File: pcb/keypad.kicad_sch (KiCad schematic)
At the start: 54 parts, among them J1 Conn_02x06_Odd_Even, SW1 SW_Push, SW10 SW_Push, SW11 SW_Push, SW12 SW_Push, SW13 SW_Push, SW14 SW_Push, SW15 SW_Push, SW16 SW_Push, SW17 SW_Push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

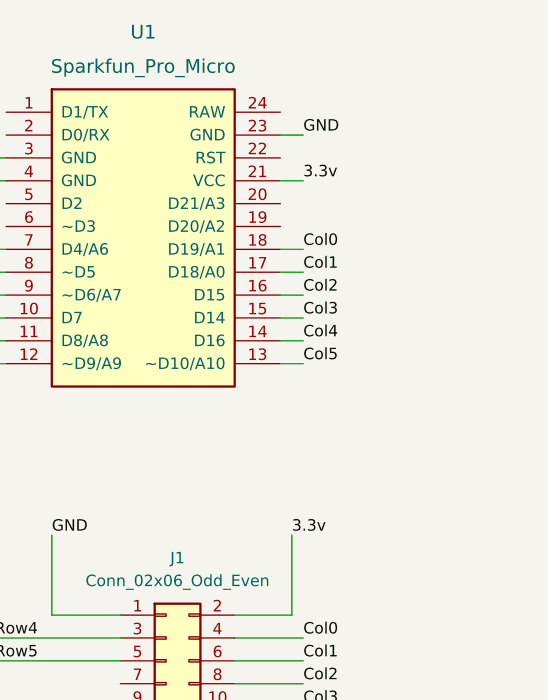
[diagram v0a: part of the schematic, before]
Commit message: - Added a reset button for the controller  - Moved the through-hole diodes to not interfere with the switches
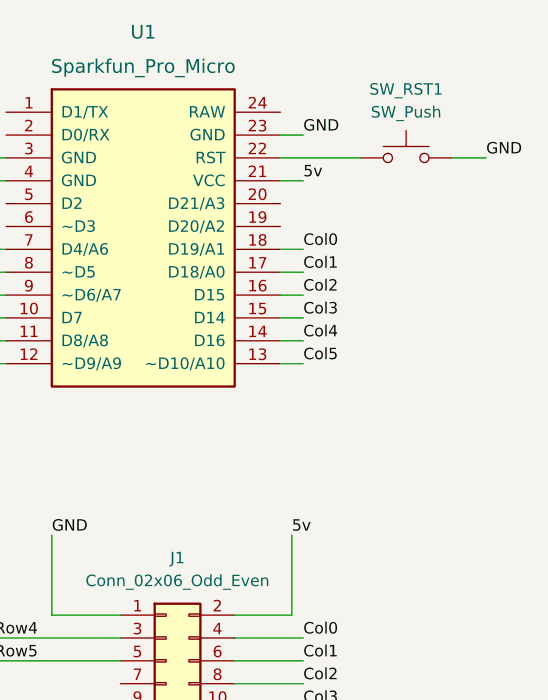
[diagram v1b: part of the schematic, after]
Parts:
- added SW_RST1: SW_Push, Button_Switch_THT:SW_PUSH_6mm_H7.3mm, symbol Switch:SW_Push
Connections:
- net GND: now also SW_RST1.2
- net at U1.22 (RST): now also SW_RST1.1
- net 3.3v renamed 5v
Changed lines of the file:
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@@
+    (stroke (width 0) (type default) (color 0 0 0 0))
+  )
+  (wire (pts (xy 204.47 36.83) (xy 208.28 36.83))
     (stroke (width 0) (type default) (color 0 0 0 0))
   )
@@
     (stroke (width 0) (type default) (color 0 0 0 0))
   )
+  (wire (pts (xy 185.42 36.83) (xy 194.31 36.83))
+    (stroke (width 0) (type default) (color 0 0 0 0))
+  )
   (wire (pts (xy 153.67 92.71) (xy 167.64 92.71))
     (stroke (width 0) (type default) (color 0 0 0 0))
@@
     (effects (font (size 1.27 1.27)) (justify left bottom))
   )
-  (label "3.3v" (at 187.96 39.37 0)
+  (label "5v" (at 187.96 39.37 0)
     (effects (font (size 1.27 1.27)) (justify left bottom))
   )
@@
     (effects (font (size 1.27 1.27)) (justify left bottom))
   )
+  (label "GND" (at 208.28 36.83 0)
+    (effects (font (size 1.27 1.27)) (justify left bottom))
+  )
   (label "Col2" (at 187.96 95.25 0)
     (effects (font (size 1.27 1.27)) (justify left bottom))
@@
     (effects (font (size 1.27 1.27)) (justify left bottom))
   )
-  (label "3.3v" (at 186.69 78.74 0)
+  (label "5v" (at 186.69 78.74 0)
     (effects (font (size 1.27 1.27)) (justify left bottom))
   )
@@
     )
     (property "Datasheet" "~" (id 3) (at 44.45 66.04 0)
+      (effects (font (size 1.27 1.27)) hide)
+    )
+    (pin "1")
+    (pin "2")
+  )
+  (symbol (lib_id "Switch:SW_Push") (at 199.39 36.83 0) (unit 1)
+    (in_bom yes) (on_board yes)
+    (property "Reference" "SW_RST1" (id 0) (at 199.39 29.21 0))
+    (property "Value" "SW_Push" (id 1) (at 199.39 31.75 0))
+    (property "Footprint" "Button_Switch_THT:SW_PUSH_6mm_H7.3mm" (id 2) (at 199.39 31.75 0)
+      (effects (font (size 1.27 1.27)) hide)
+    )
+    (property "Datasheet" "~" (id 3) (at 199.39 31.75 0)
       (effects (font (size 1.27 1.27)) hide)
     )
@@
       (reference "SW_C1") (unit 1) (value "SW_Push") (footprint "Button_Switch_THT:SW_PUSH_6mm_H7.3mm")
     )
+    (path "/5b2e8b2b-3715-432b-9074-5bf4a85d40d6"
+      (reference "SW_RST1") (unit 1) (value "SW_Push") (footprint "Button_Switch_THT:SW_PUSH_6mm_H7.3mm")
+    )
     (path "/7127a1b5-5c6f-4116-ab41-a3e00f7558f8"

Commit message: - Switched to the KB2040  - Modified the pin header to remove some silk screen sections
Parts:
- removed U1: Sparkfun_Pro_Micro, Arduino:Sparkfun_Pro_Micro, symbol Arduino:Sparkfun_Pro_Micro
- added U1: kb2040, kb2040:kb2040, symbol kb2040:kb2040
- J1: footprint Connector_PinHeader_2.54mm:PinHeader_2x06_P2.54mm_Horizontal -> keypad:PinHeader_2x06_P2.54mm_Horizontal
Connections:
- net Col0: now also U1.21 (A1/27)
- net Col1: now also U1.22 (A0/26)
- net Col2: now also U1.23 (SCK/18)
- net Col3: now also U1.24 (MISO/20)
- net Col4: now also U1.25 (MOSI/19)
- net Col5: now also U1.26 (D10)
- net GND: now also U1.16 (GND), U1.4 (GND), U1.5 (GND)
- net Row0: now also U1.13 (D9)
- net Row1: now also U1.12 (D8)
- net Row2: now also U1.11 (D7)
- net Row3: now also U1.10 (D6)
- net Row4: now also U1.9 (D5)
- net Row5: now also U1.8 (D4)
- net at SW_RST1.1: now also U1.17 (RESET)
- net 5v renamed 3.3v
- net 3.3v: now also U1.18 (3.3v)

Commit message: Moved necessary symbols into the project library  - (I don't know if this comes with license issues; if there's a problem let me know and I can remove the symbols)
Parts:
- SW1, SW10, SW11, SW12, SW13, SW14, SW16, SW17, SW18, SW2, SW21, SW3, SW4, SW5, SW6, SW7, SW8, SW9: footprint MX_Only:MXOnly-1U-Hotswap -> keypad:MXOnly-1U-Hotswap
- SW15, SW19: footprint MX_Only:MXOnly-1.25U-Hotswap -> keypad:MXOnly-1.25U-Hotswap
- SW20, SW22: footprint MX_Only:MXOnly-2U-Hotswap -> keypad:MXOnly-2U-Hotswap
- U1: footprint kb2040:kb2040 -> keypad:kb2040; symbol kb2040:kb2040 -> keypad:kb2040

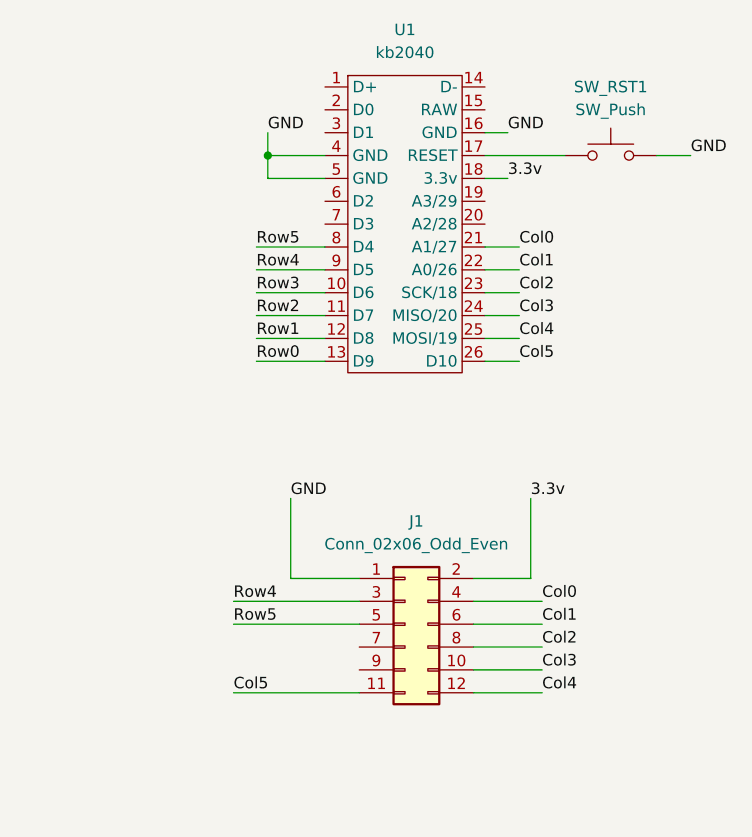
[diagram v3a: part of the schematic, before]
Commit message: - Marked NC pins  - Updated diode symbols
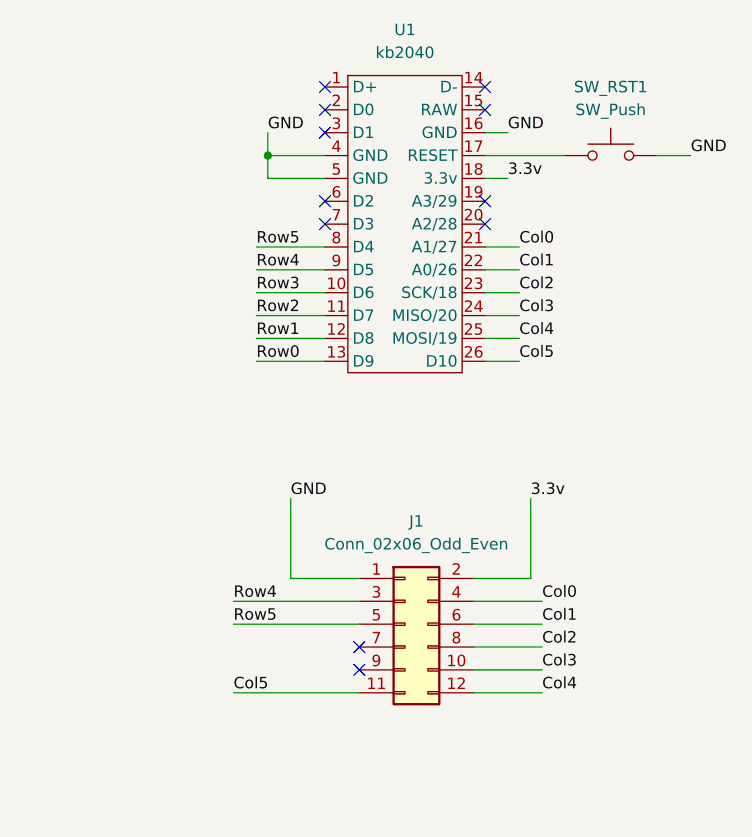
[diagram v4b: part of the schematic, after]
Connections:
- no-connect marks 0 -> 11
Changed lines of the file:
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@@
   (junction (at 100.33 59.69) (diameter 0) (color 0 0 0 0)
   )
+  (no_connect (at 167.64 97.79))
+  (no_connect (at 163.83 33.02))
+  (no_connect (at 163.83 38.1))
+  (no_connect (at 163.83 35.56))
+  (no_connect (at 163.83 48.26))
+  (no_connect (at 181.61 45.72))
+  (no_connect (at 163.83 45.72))
+  (no_connect (at 181.61 33.02))
+  (no_connect (at 181.61 48.26))
+  (no_connect (at 167.64 95.25))
+  (no_connect (at 181.61 35.56))
   (wire (pts (xy 71.12 53.34) (xy 67.31 53.34))
     (stroke (width 0) (type default) (color 0 0 0 0))
@@
     (effects (font (size 1.27 1.27)) (justify left bottom))
   )
-  (symbol (lib_id "Diode:1N4148") (at 120.65 105.41 0) (unit 1)
+  (symbol (lib_name "1N4148_10") (lib_id "Diode:1N4148") (at 120.65 105.41 0) (unit 1)
     (in_bom yes) (on_board yes) (fields_autoplaced)
     (property "Reference" "D18" (id 0) (at 120.65 99.06 0))
@@
     (pin "2")
   )
-  (symbol (lib_id "Diode:1N4148") (at 74.93 80.01 0) (unit 1)
+  (symbol (lib_name "1N4148_5") (lib_id "Diode:1N4148") (at 74.93 80.01 0) (unit 1)
     (in_bom yes) (on_board yes) (fields_autoplaced)
     (property "Reference" "D9" (id 0) (at 74.93 73.66 0))
@@
     (pin "2")
   )
-  (symbol (lib_id "Diode:1N4148") (at 105.41 53.34 0) (unit 1)
+  (symbol (lib_name "1N4148_2") (lib_id "Diode:1N4148") (at 105.41 53.34 0) (unit 1)
     (in_bom yes) (on_board yes) (fields_autoplaced)
     (property "Reference" "D5" (id 0) (at 105.41 46.99 0))
@@
     (pin "2")
   )
-  (symbol (lib_id "Diode:1N4148") (at 44.45 105.41 0) (unit 1)
+  (symbol (lib_name "1N4148_18") (lib_id "Diode:1N4148") (at 44.45 105.41 0) (unit 1)
     (in_bom yes) (on_board yes) (fields_autoplaced)
     (property "Reference" "D13" (id 0) (at 44.45 99.06 0))
@@
     (pin "2")
   )
-  (symbol (lib_id "Diode:1N4148") (at 105.41 105.41 0) (unit 1)
+  (symbol (lib_name "1N4148_11") (lib_id "Diode:1N4148") (at 105.41 105.41 0) (unit 1)
     (in_bom yes) (on_board yes) (fields_autoplaced)
     (property "Reference" "D17" (id 0) (at 105.41 99.06 0))
@@
     (pin "2")
   )
-  (symbol (lib_id "Diode:1N4148") (at 59.69 105.41 0) (unit 1)
+  (symbol (lib_name "1N4148_8") (lib_id "Diode:1N4148") (at 59.69 105.41 0) (unit 1)
     (in_bom yes) (on_board yes) (fields_autoplaced)
     (property "Reference" "D14" (id 0) (at 59.69 99.06 0))
@@
     (pin "2")
   )
-  (symbol (lib_id "Diode:1N4148") (at 120.65 80.01 0) (unit 1)
+  (symbol (lib_name "1N4148_6") (lib_id "Diode:1N4148") (at 120.65 80.01 0) (unit 1)
     (in_bom yes) (on_board yes) (fields_autoplaced)
     (property "Reference" "D12" (id 0) (at 120.65 73.66 0))
@@
     (pin "2")
   )
-  (symbol (lib_id "Diode:1N4148") (at 74.93 105.41 0) (unit 1)
+  (symbol (lib_name "1N4148_12") (lib_id "Diode:1N4148") (at 74.93 105.41 0) (unit 1)
     (in_bom yes) (on_board yes) (fields_autoplaced)
     (property "Reference" "D15" (id 0) (at 74.93 99.06 0))
@@
     (pin "2")
   )
-  (symbol (lib_id "Diode:1N4148") (at 74.93 130.81 0) (unit 1)
+  (symbol (lib_name "1N4148_19") (lib_id "Diode:1N4148") (at 74.93 130.81 0) (unit 1)
     (in_bom yes) (on_board yes) (fields_autoplaced)
     (property "Reference" "D21" (id 0) (at 74.93 124.46 0))
@@
     )
   )
-  (symbol (lib_id "Diode:1N4148") (at 59.69 80.01 0) (unit 1)
+  (symbol (lib_name "1N4148_13") (lib_id "Diode:1N4148") (at 59.69 80.01 0) (unit 1)
     (in_bom yes) (on_board yes) (fields_autoplaced)
     (property "Reference" "D8" (id 0) (at 59.69 73.66 0))
@@
     (pin "2")
   )
-  (symbol (lib_id "Diode:1N4148") (at 90.17 53.34 0) (unit 1)
+  (symbol (lib_name "1N4148_3") (lib_id "Diode:1N4148") (at 90.17 53.34 0) (unit 1)
     (in_bom yes) (on_board yes) (fields_autoplaced)
     (property "Reference" "D4" (id 0) (at 90.17 46.99 0))
@@
     (pin "2")
   )
-  (symbol (lib_id "Diode:1N4148") (at 44.45 53.34 0) (unit 1)
+  (symbol (lib_name "1N4148_16") (lib_id "Diode:1N4148") (at 44.45 53.34 0) (unit 1)
     (in_bom yes) (on_board yes) (fields_autoplaced)
     (property "Reference" "D1" (id 0) (at 44.45 46.99 0))
@@
     (pin "2")
   )
-  (symbol (lib_id "Diode:1N4148") (at 74.93 53.34 0) (unit 1)
+  (symbol (lib_name "1N4148_15") (lib_id "Diode:1N4148") (at 74.93 53.34 0) (unit 1)
     (in_bom yes) (on_board yes) (fields_autoplaced)
     (property "Reference" "D3" (id 0) (at 74.93 46.99 0))
@@
     (pin "9")
   )
-  (symbol (lib_id "Diode:1N4148") (at 120.65 130.81 0) (unit 1)
+  (symbol (lib_name "1N4148_23") (lib_id "Diode:1N4148") (at 120.65 130.81 0) (unit 1)
     (in_bom yes) (on_board yes) (fields_autoplaced)
     (property "Reference" "D24" (id 0) (at 120.65 124.46 0))
@@
     (pin "2")
   )
-  (symbol (lib_id "Diode:1N4148") (at 59.69 53.34 0) (unit 1)
+  (symbol (lib_name "1N4148_14") (lib_id "Diode:1N4148") (at 59.69 53.34 0) (unit 1)
     (in_bom yes) (on_board yes) (fields_autoplaced)
     (property "Reference" "D2" (id 0) (at 59.69 46.99 0))
@@
     (pin "2")
   )
-  (symbol (lib_id "Diode:1N4148") (at 90.17 130.81 0) (unit 1)
+  (symbol (lib_name "1N4148_22") (lib_id "Diode:1N4148") (at 90.17 130.81 0) (unit 1)
     (in_bom yes) (on_board yes) (fields_autoplaced)
     (property "Reference" "D22" (id 0) (at 90.17 124.46 0))
@@
     (pin "2")
   )
-  (symbol (lib_id "Diode:1N4148") (at 90.17 105.41 0) (unit 1)
+  (symbol (lib_name "1N4148_9") (lib_id "Diode:1N4148") (at 90.17 105.41 0) (unit 1)
     (in_bom yes) (on_board yes) (fields_autoplaced)
     (property "Reference" "D16" (id 0) (at 90.17 99.06 0))
@@
     (pin "2")
   )
-  (symbol (lib_id "Diode:1N4148") (at 105.41 80.01 0) (unit 1)
+  (symbol (lib_name "1N4148_1") (lib_id "Diode:1N4148") (at 105.41 80.01 0) (unit 1)
     (in_bom yes) (on_board yes) (fields_autoplaced)
     (property "Reference" "D11" (id 0) (at 105.41 73.66 0))
@@
     (pin "2")
   )
-  (symbol (lib_id "Diode:1N4148") (at 59.69 130.81 0) (unit 1)
+  (symbol (lib_name "1N4148_21") (lib_id "Diode:1N4148") (at 59.69 130.81 0) (unit 1)
     (in_bom yes) (on_board yes) (fields_autoplaced)
     (property "Reference" "D20" (id 0) (at 59.69 124.46 0))
@@
     (pin "2")
   )
-  (symbol (lib_id "Diode:1N4148") (at 90.17 80.01 0) (unit 1)
+  (symbol (lib_name "1N4148_4") (lib_id "Diode:1N4148") (at 90.17 80.01 0) (unit 1)
     (in_bom yes) (on_board yes) (fields_autoplaced)
     (property "Reference" "D10" (id 0) (at 90.17 73.66 0))
@@
     (pin "2")
   )
-  (symbol (lib_id "Diode:1N4148") (at 120.65 53.34 0) (unit 1)
+  (symbol (lib_name "1N4148_7") (lib_id "Diode:1N4148") (at 120.65 53.34 0) (unit 1)
     (in_bom yes) (on_board yes) (fields_autoplaced)
     (property "Reference" "D6" (id 0) (at 120.65 46.99 0))
@@
     (pin "2")
   )
-  (symbol (lib_id "Diode:1N4148") (at 44.45 80.01 0) (unit 1)
+  (symbol (lib_name "1N4148_17") (lib_id "Diode:1N4148") (at 44.45 80.01 0) (unit 1)
     (in_bom yes) (on_board yes) (fields_autoplaced)
     (property "Reference" "D7" (id 0) (at 44.45 73.66 0))
@@
     (pin "2")
   )
-  (symbol (lib_id "Diode:1N4148") (at 44.45 130.81 0) (unit 1)
+  (symbol (lib_name "1N4148_20") (lib_id "Diode:1N4148") (at 44.45 130.81 0) (unit 1)
     (in_bom yes) (on_board yes) (fields_autoplaced)
     (property "Reference" "D19" (id 0) (at 44.45 124.46 0))
